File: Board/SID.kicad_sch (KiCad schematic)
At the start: 25 parts, among them IC25 74139N, J9 Conn_01x01_Pin

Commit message: more work on r1.3
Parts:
- added C161, C162, C163, C164: 2200, cbm_ultipet_v1:C025-025X050, symbol cbm_ultipet_v1-eagle-import:C-EU025-025X050
- added JP15, JP9: JP1E, cbm_ultipet_v1:JP1, symbol cbm_ultipet_v1-eagle-import:JP1E
- added R45, R46: 1k, cbm_ultipet_v1:0207_10, symbol cbm_ultipet_v1-eagle-import:R-EU_0207/10
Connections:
- net GND: now also C161.1, C162.1, C163.1, C164.1, R45.2, R46.2
- net POTAX: now also C161.2
- net POTAY: now also C162.2
- net POTBX: now also C163.2
- net POTBY: now also C164.2
- net SIDLEFT: now also JP15.1
- net SIDRIGHT: now also JP9.1
- new net: JP9.2, R45.1
- new net: JP15.2, R46.1
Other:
- note added: "C161-C164: optional only if paddles are used"
- note added: "CBM-ULTIPET-1.3A-20250806"
- note added: "CBM-ULTIPET-V1.3A"
- note added: "V1.3A: - add optional 1k pulldown on audio out (seems to be necessary for original SID) - add optional paddle caps"
- note removed: "CBM-ULTIPET-1.0A-20240331"
- note removed: "CBM-ULTIPET-V1.1A"

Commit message: rename U refs to UX*
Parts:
- renumbered U$22 to UX22, U$23 to UX23
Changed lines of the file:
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@@
 		(on_board yes)
 		(dnp no)
-		(property "Reference" "U$23"
+		(property "Reference" "UX23"
 			(at 220.98 157.48 0)
 			(effects
@@
 			(project "cbm_ultipet_v1"
 				(path "/4dd2dd78-173f-4b46-8cce-4ed940435c94/ef987787-576d-4ba9-8915-c171f881d1b8"
-					(reference "U$23")
+					(reference "UX23")
 					(unit 1)
 				)
@@
 		(on_board yes)
 		(dnp no)
-		(property "Reference" "U$22"
+		(property "Reference" "UX22"
 			(at 220.98 91.44 0)
 			(effects
@@
 			(project "cbm_ultipet_v1"
 				(path "/4dd2dd78-173f-4b46-8cce-4ed940435c94/ef987787-576d-4ba9-8915-c171f881d1b8"
-					(reference "U$22")
-					(unit 1)
-				)
+					(reference "UX22")
+					(unit 1)
+				)

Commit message: some layout fixes, more parts
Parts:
- C72: footprint cbm_ultipet_v1:E2,5-7 -> cbm_ultipet_v1:E2,5-6
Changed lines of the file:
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@@
 			)
 		)
-		(property "Footprint" "cbm_ultipet_v1:E2,5-7"
+		(property "Footprint" "cbm_ultipet_v1:E2,5-6"
 			(at 50.8 175.26 0)
 			(effects

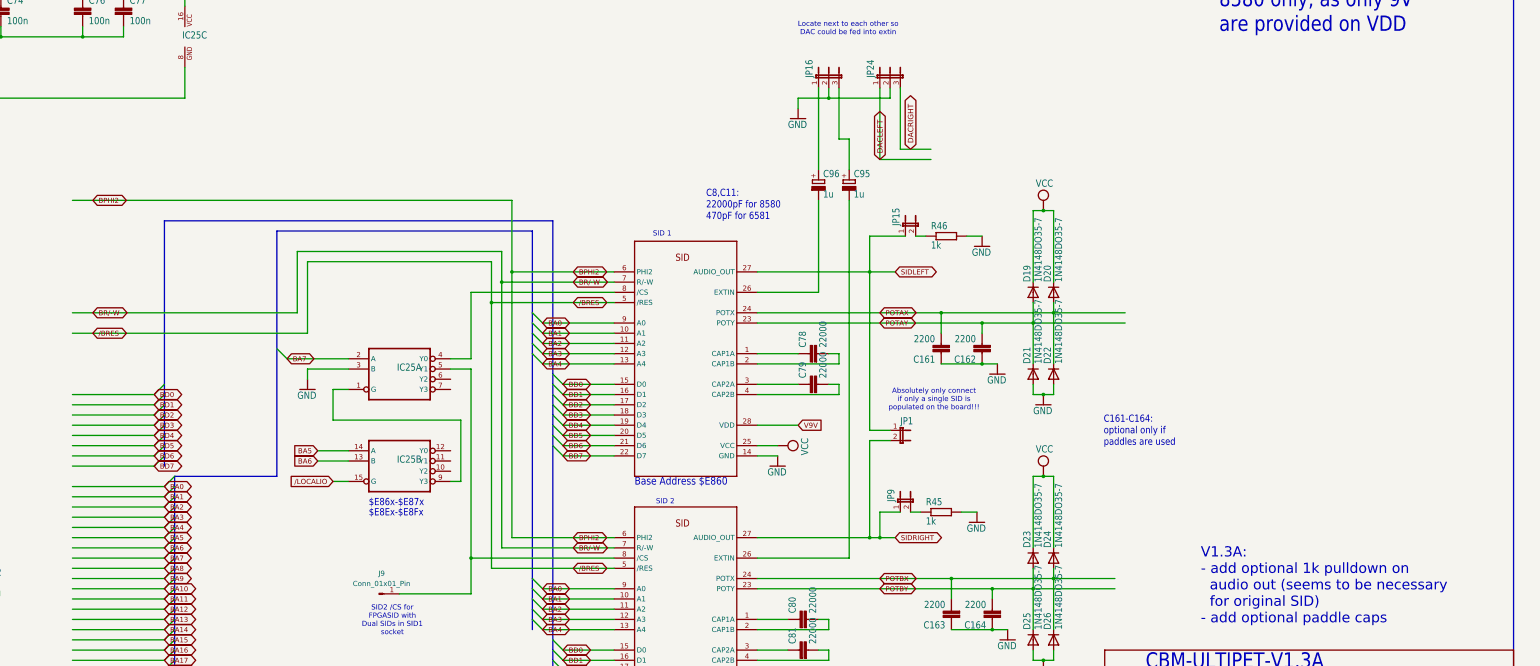
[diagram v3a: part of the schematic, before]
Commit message: adding SID mirroring to schem
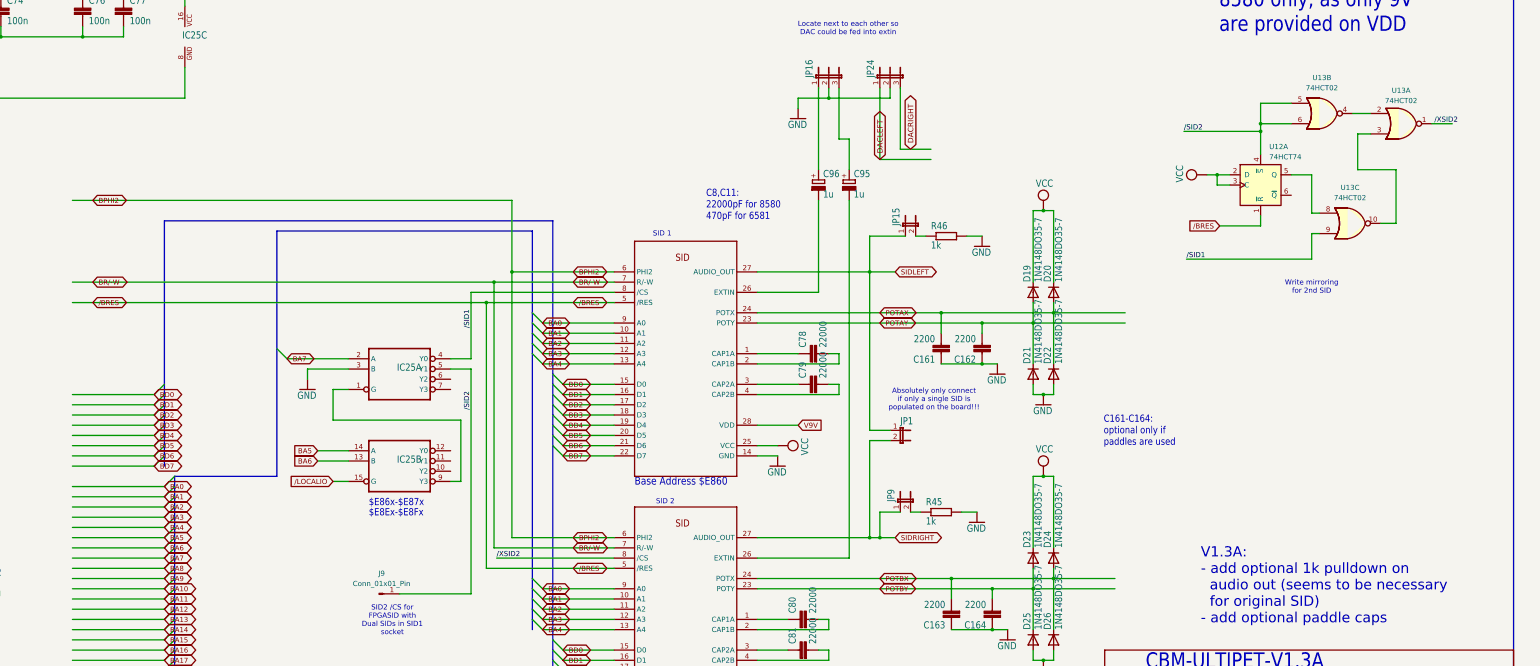
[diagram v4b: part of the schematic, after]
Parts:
- added U12: 74HCT74, Package_SO:SOIC-14_3.9x8.7mm_P1.27mm, symbol 74xx:74HCT74
- added U13: 74HCT02, Package_SO:SOIC-14_3.9x8.7mm_P1.27mm, symbol 74xx:74HCT02
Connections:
- net VCC: now also U12.2 (D), U12.3 (C)
- net /SID2: now reaches IC25.5 (Y1), J9.1 (Pin_1)
- net /SID2: now also U12.4 (~{S}), U13.5, U13.6; no longer UX23.8 (/CS)
- net /SID1: now reaches IC25.4 (Y0), UX22.8 (/CS)
- net /SID1: now also U13.9
- new net: U13.10, U13.3
- new net: U12.5 (Q), U13.8
- new net: U13.2, U13.4
- new net /BRES: U12.1 (~{R})
- new net /XSID2: U13.1, UX23.8 (/CS)
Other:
- note added: "Write mirroring for 2nd SID"

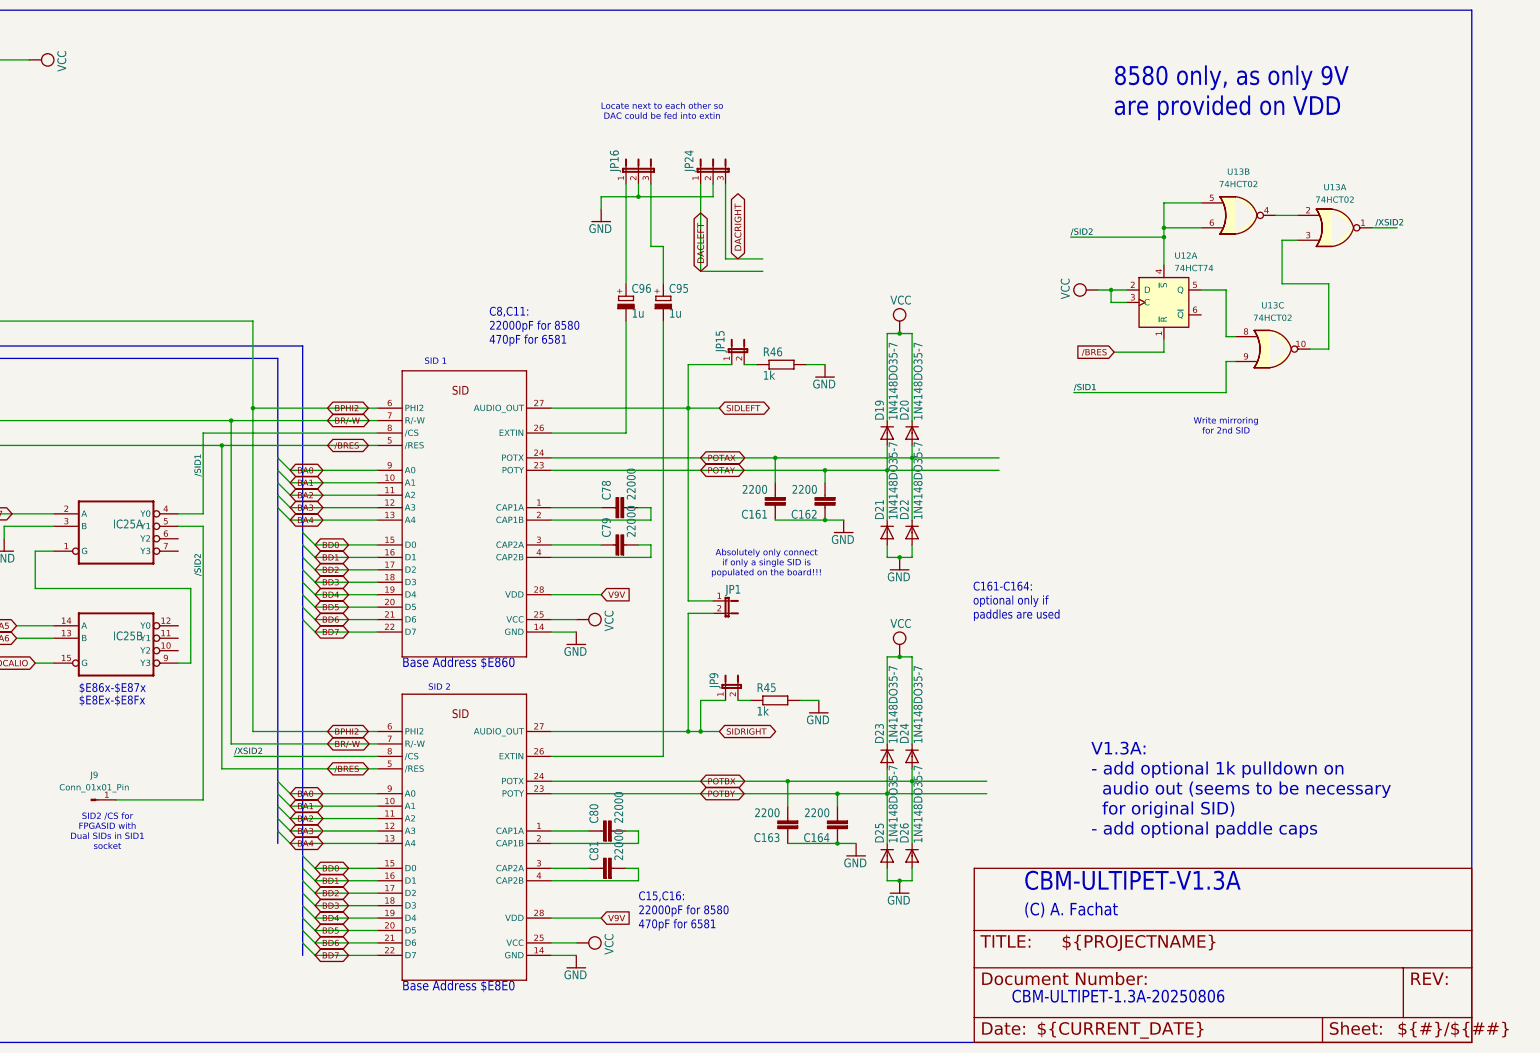
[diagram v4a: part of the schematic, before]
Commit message: add C64 restore
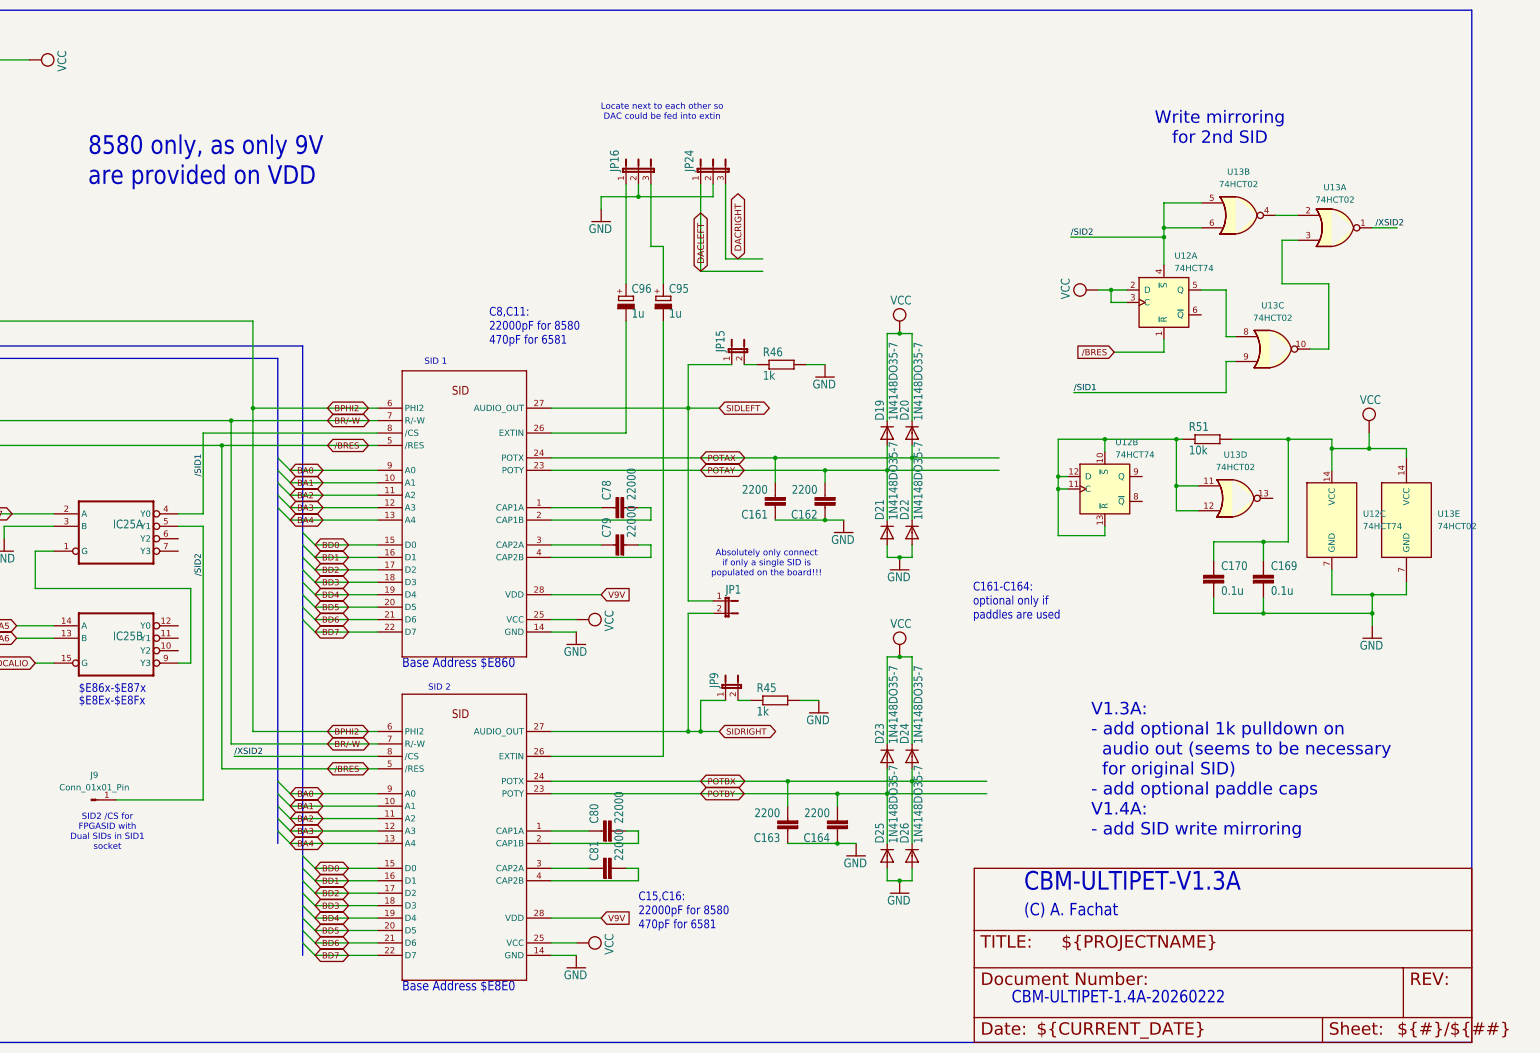
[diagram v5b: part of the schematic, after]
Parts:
- added C169, C170: 0.1u, cbm_ultipet_v1:C0603, symbol cbm_ultipet_v1-eagle-import:C-EUC0603
- added R51: 10k, Resistor_SMD:R_0805_2012Metric_Pad1.20x1.40mm_HandSolder, symbol csa_ultracpu-eagle-import:R-EU_0207/2V
- added unit 3 of U12
- added unit 1 of U12
- added unit 4 of U13
- added unit 3 of U13
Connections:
- net GND: now also U13.7 (GND), C169.2, C170.2, U12.7 (GND)
- net VCC: now also U13.14 (VCC), C169.1, C170.1, R51.2, U12.14 (VCC), U12.2 (D), U12.3 (C); no longer U12.2 (D), U12.3 (C)
- net /BRES: now also U12.1 (~{R}); no longer U12.1 (~{R})
- net /SID1: now also U13.9; no longer U13.9
- net /SID2: now also U12.4 (~{S}); no longer U12.4 (~{S})
- net at U13.3: now also U13.10; no longer U13.10
- new net: R51.1, U12.10 (~{S}), U12.11 (C), U12.12 (D), U12.13 (~{R}), U13.11, U13.12
- new net: U12.5 (Q), U13.8
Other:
- note added: "CBM-ULTIPET-1.4A-20260222"
- note added: "V1.3A: - add optional 1k pulldown on audio out (seems to be necessary for original SID) - add optional paddle caps V1.4A: - add SID write mirroring"
- note removed: "CBM-ULTIPET-1.3A-20250806"
- note removed: "V1.3A: - add optional 1k pulldown on audio out (seems to be necessary for original SID) - add optional paddle caps"
- moved on the sheet: U12B
